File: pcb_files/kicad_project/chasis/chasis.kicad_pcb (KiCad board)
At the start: 2 copper layers, 172.8 x 166.9 mm, 16 parts, among them J1 Conn_01x01_Pin, J2 Conn_01x08_Pin, J3 Conn_01x08_Pin

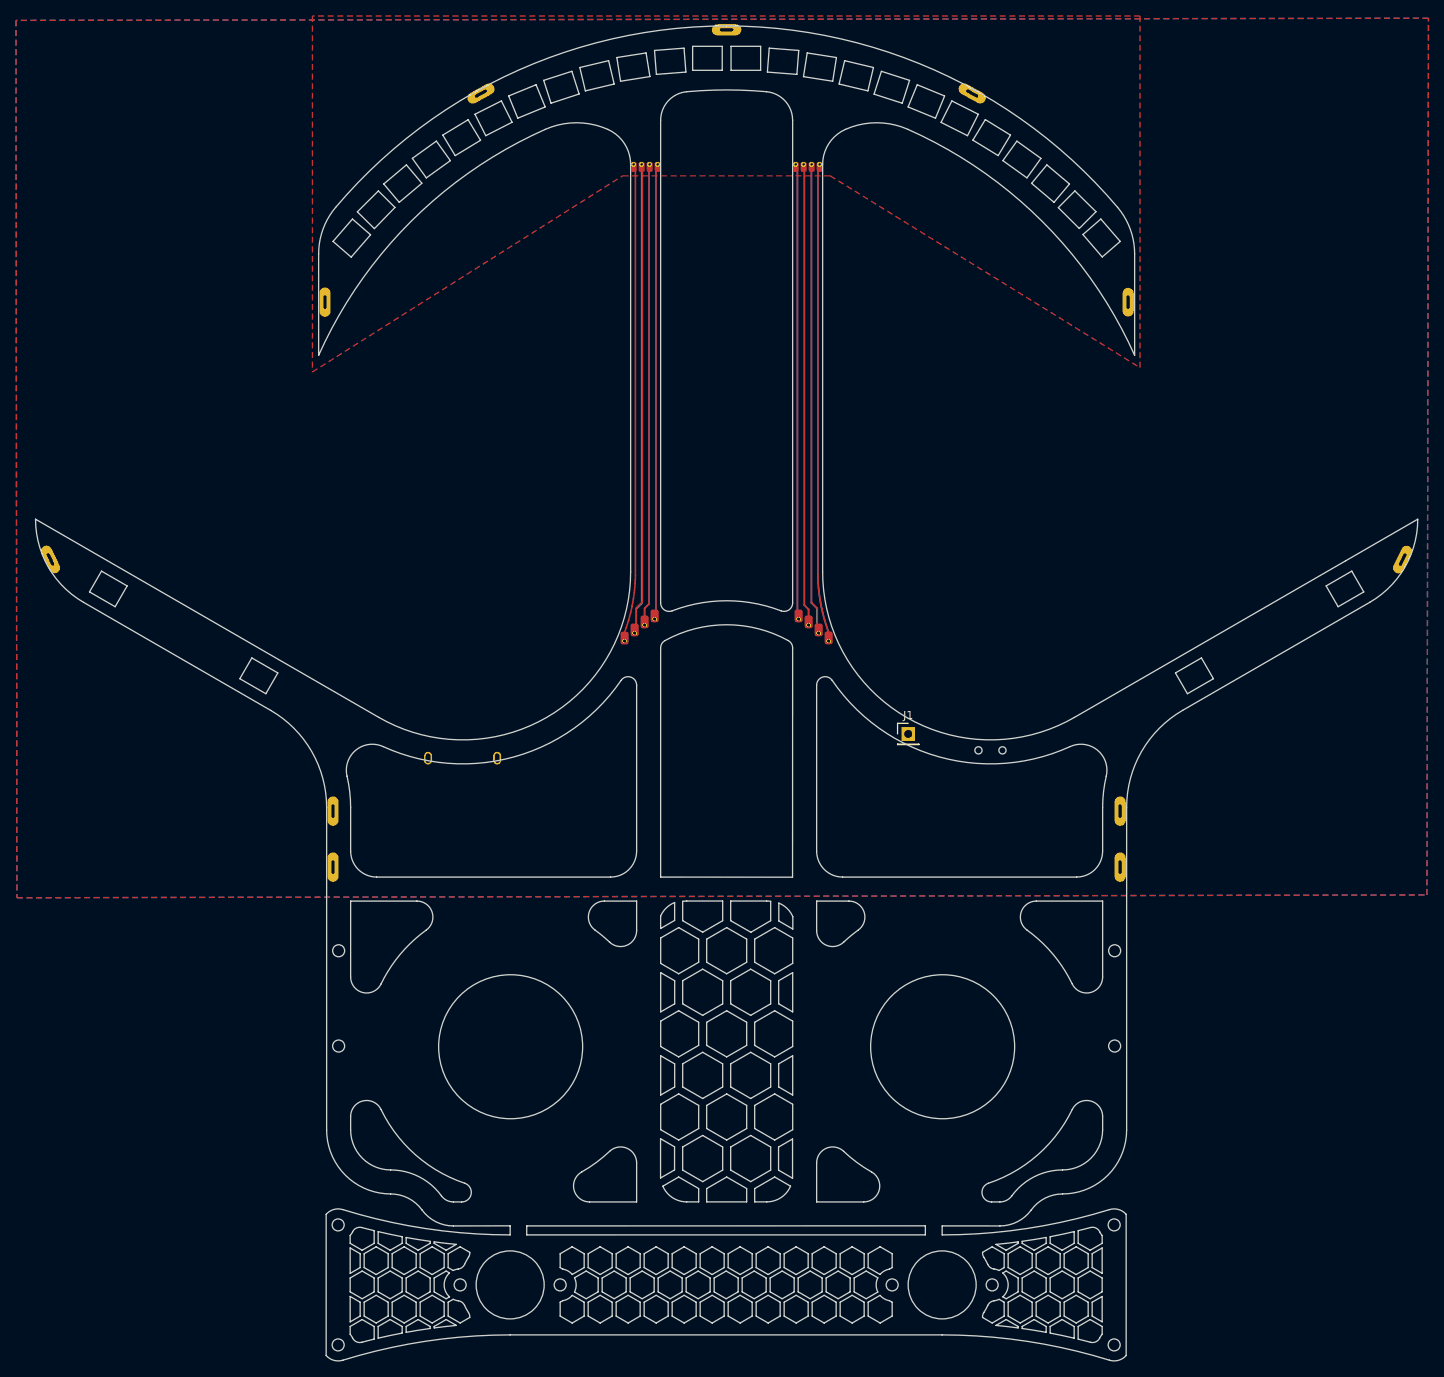
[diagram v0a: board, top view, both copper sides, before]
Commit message: Finaliza la PCB del chasis
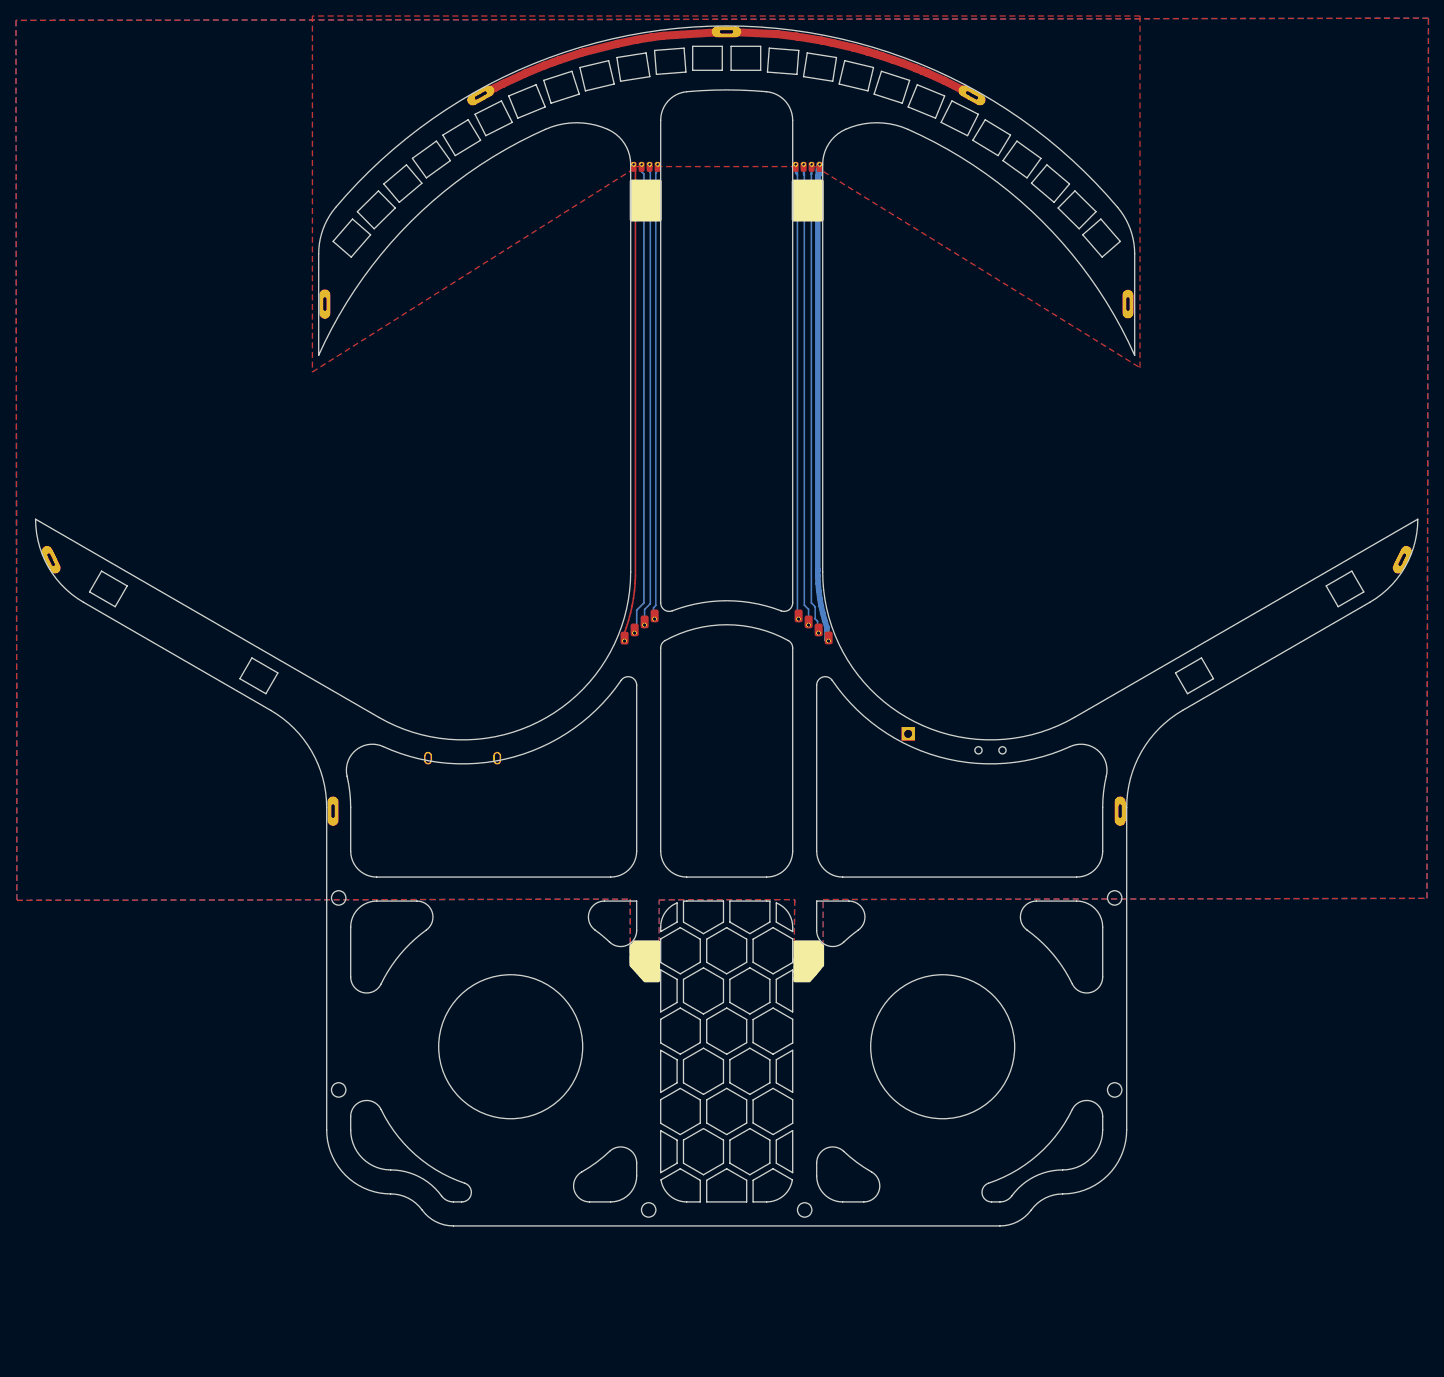
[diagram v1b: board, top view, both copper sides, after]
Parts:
- removed the ? at (56.6, 54.4)
- removed the ? at (157.0, 54.4)
- removed the ? at (57.6, 125.0)
- removed the ? at (156.0, 125.0)
- removed the ? at (76.1, 28.3)
- removed the ? at (137.5, 28.3)
- removed the ? at (57.6, 118.0)
- removed the ? at (22.3, 86.6)
- removed the ? at (156.0, 118.0)
- removed the ? at (191.3, 86.6)
- added ?: , , F.Cu at (56.6, 54.6)
- added ?: , , F.Cu at (191.3, 86.6)
- added ?: , , F.Cu at (22.4, 86.6)
- added ?: , , F.Cu at (57.6, 118.0)
- added ?: , , F.Cu at (76.1, 28.6)
- added ?: , , F.Cu at (156.0, 118.0)
- added ?: , , F.Cu at (137.5, 28.6)
- added ?: , , B.Cu at (157.0, 54.6)
- J1: value Conn_01x01_Pin -> Conn_01x08_Pin; footprint Connector_PinHeader_2.54mm:PinHeader_1x01_P2.54mm_Vertical -> custom_footprints:DragonBot_pads_main
- J2: footprint custom_footprints:DragonBot_pads_main -> custom_footprints:DragonBot_pads_morro
- J3: value Conn_01x08_Pin -> Conn_01x01_Pin; footprint custom_footprints:DragonBot_pads_morro -> Connector_PinHeader_2.54mm:PinHeader_1x01_P2.54mm_Vertical
- moved J3 74.7 mm to (129.5, 108.4)
- moved J2 59.2 mm to (106.9, 37.2)
- moved J1 25.7 mm to (106.8, 96.4)
- moved JP2 0.24 mm to (107.5, 20.6)
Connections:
- J2 pad 2: Net-(J2-Pin_2) -> Net-(J1-Pin_2)
- J2 pad 3: Net-(J2-Pin_3) -> Net-(J1-Pin_3)
- J2 pad 4: Net-(J2-Pin_4) -> Net-(J1-Pin_4)
- J2 pad 5: Net-(J2-Pin_5) -> Net-(J1-Pin_5)
- J2 pad 6: Net-(J2-Pin_6) -> Net-(J1-Pin_6)
- J2 pad 7: Net-(J2-Pin_7) -> Net-(J1-Pin_7)
- J2 pad 8: Net-(J2-Pin_8) -> Net-(J1-Pin_8)
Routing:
- net Net-(J2-Pin_2): track 118.0 -> 0.00 mm
- net Net-(J2-Pin_7): track 117.9 -> 0.00 mm
- net Net-(J2-Pin_6): track 115.7 -> 0.00 mm
- net Net-(J2-Pin_3): track 115.7 -> 0.00 mm
- net Net-(J2-Pin_5): track 113.7 -> 0.00 mm
- net Net-(J2-Pin_4): track 113.5 -> 0.00 mm
- net Net-(J1-Pin_8): track 0.00 -> 61.8 mm
- net Net-(J1-Pin_2): track 0.00 -> 60.5 mm
- net Net-(J1-Pin_7): track 0.00 -> 60.2 mm
- net Net-(J1-Pin_6): track 0.00 -> 59.3 mm
- net Net-(J1-Pin_3): track 0.00 -> 58.9 mm
- net Net-(J1-Pin_5): track 0.00 -> 58.5 mm
- net Net-(J1-Pin_4): track 0.00 -> 58.3 mm
- net Net-(J2-Pin_8): track 119.5 -> 64.2 mm
- net GND: vias 0 -> 26
- added copper zone on F.Cu, net (none)
- removed copper zone on F.Cu, net Net-(J2-Pin_8)
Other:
- board size 172.8 x 166.9 mm -> 172.8 x 150 mm
